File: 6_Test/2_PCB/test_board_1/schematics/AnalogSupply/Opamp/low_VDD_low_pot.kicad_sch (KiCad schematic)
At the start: 4 parts, among them U1 ADA4807-1AKSZ-R7

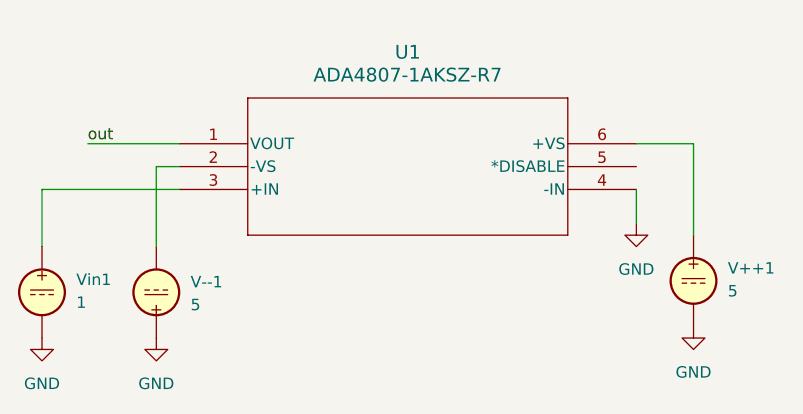
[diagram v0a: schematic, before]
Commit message: progress on op amp. ldo done
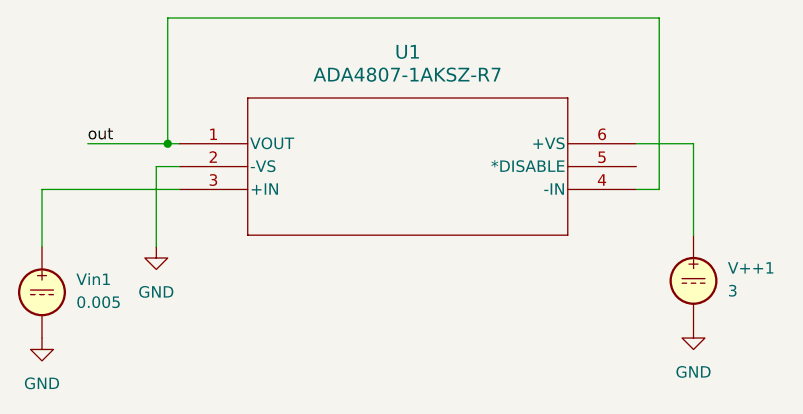
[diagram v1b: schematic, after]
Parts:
- removed V--1: 5, symbol Simulation_SPICE:VDC
- V++1: value 5 -> 3
- Vin1: value 1 -> 0.005
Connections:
- net GND: now also U1.2 (-VS); no longer U1.4 (-IN)
- net out: now also U1.4 (-IN)
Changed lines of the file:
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@@
 	(generator_version "8.0")
 	(paper "A4")
+	(junction
+		(at 125.73 104.14)
+		(diameter 0)
+		(color 0 0 0 0)
+	)
 	(wire
 		(pts
@@
 	(wire
 		(pts
+			(xy 180.34 109.22) (xy 177.8 109.22)
+		)
+		(stroke
+			(width 0)
+			(type default)
+		)
+	)
+	(wire
+		(pts
+			(xy 180.34 90.17) (xy 180.34 109.22)
+		)
+		(stroke
+			(width 0)
+			(type default)
+		)
+	)
+	(wire
+		(pts
 			(xy 124.46 106.68) (xy 127 106.68)
 		)
@@
 	(wire
 		(pts
+			(xy 125.73 104.14) (xy 125.73 90.17)
+		)
+		(stroke
+			(width 0)
+			(type default)
+		)
+	)
+	(wire
+		(pts
 			(xy 184.15 104.14) (xy 184.15 114.3)
 		)
@@
 	(wire
 		(pts
-			(xy 116.84 104.14) (xy 127 104.14)
+			(xy 116.84 104.14) (xy 125.73 104.14)
 		)
 		(stroke
@@
 	(wire
 		(pts
-			(xy 177.8 113.03) (xy 177.8 109.22)
-		)
-		(stroke
-			(width 0)
-			(type default)
-		)
-	)
-	(wire
-		(pts
 			(xy 111.76 109.22) (xy 111.76 115.57)
+		)
+		(stroke
+			(width 0)
+			(type default)
+		)
+	)
+	(wire
+		(pts
+			(xy 125.73 104.14) (xy 127 104.14)
+		)
+		(stroke
+			(width 0)
+			(type default)
+		)
+	)
+	(wire
+		(pts
+			(xy 125.73 90.17) (xy 180.34 90.17)
 		)
 		(stroke
@@
 			)
 		)
-		(property "Value" "5"
+		(property "Value" "3"
 			(at 187.96 120.5201 0)
 			(effects
@@
 				(path "/95e5dcee-77e4-4cc3-9d7c-d0dc3cd96a78"
 					(reference "V++1")
-					(unit 1)
-				)
-			)
-		)
-	)
-	(symbol
-		(lib_id "Simulation_SPICE:VDC")
-		(at 124.46 120.65 180)
-		(unit 1)
-		(exclude_from_sim no)
-		(in_bom yes)
-		(on_board yes)
-		(dnp no)
-		(fields_autoplaced yes)
-		(property "Reference" "V--1"
-			(at 128.27 119.5097 0)
-			(effects
-				(font
-					(size 1.27 1.27)
-				)
-				(justify right)
-			)
-		)
-		(property "Value" "5"
-			(at 128.27 122.0497 0)
-			(effects
-				(font
-					(size 1.27 1.27)
-				)
-				(justify right)
-			)
-		)
-		(property "Footprint" ""
-			(at 124.46 120.65 0)
-			(effects
-				(font
-					(size 1.27 1.27)
-				)
-				(hide yes)
-			)
-		)
-		(property "Datasheet" "https://ngspice.sourceforge.io/docs/ngspice-html-manual/manual.xhtml#sec_Independent_Sources_for"
-			(at 124.46 120.65 0)
-			(effects
-				(font
-					(size 1.27 1.27)
-				)
-				(hide yes)
-			)
-		)
-		(property "Description" "Voltage source, DC"
-			(at 124.46 120.65 0)
-			(effects
-				(font
-					(size 1.27 1.27)
-				)
-				(hide yes)
-			)
-		)
-		(property "Sim.Pins" "1=+ 2=-"
-			(at 124.46 120.65 0)
-			(effects
-				(font
-					(size 1.27 1.27)
-				)
-				(hide yes)
-			)
-		)
-		(property "Sim.Type" "DC"
-			(at 124.46 120.65 0)
-			(effects
-				(font
-					(size 1.27 1.27)
-				)
-				(hide yes)
-			)
-		)
-		(property "Sim.Device" "V"
-			(at 124.46 120.65 0)
-			(effects
-				(font
-					(size 1.27 1.27)
-				)
-				(justify left)
-				(hide yes)
-			)
-		)
-		(pin "2"
-		)
-		(pin "1"
-		)
-		(instances
-			(project "Opamp"
-				(path "/95e5dcee-77e4-4cc3-9d7c-d0dc3cd96a78"
-					(reference "V--1")
-					(unit 1)
-				)
-			)
-		)
-	)
-	(symbol
-		(lib_id "power:GND")
-		(at 177.8 113.03 0)
-		(unit 1)
-		(exclude_from_sim no)
-		(in_bom yes)
-		(on_board yes)
-		(dnp no)
-		(fields_autoplaced yes)
-		(property "Reference" "#PWR03"
-			(at 177.8 119.38 0)
-			(effects
-				(font
-					(size 1.27 1.27)
-				)
-				(hide yes)
-			)
-		)
-		(property "Value" "GND"
-			(at 177.8 118.11 0)
-			(effects
-				(font
-					(size 1.27 1.27)
-				)
-			)
-		)
-		(property "Footprint" ""
-			(at 177.8 113.03 0)
-			(effects
-				(font
-					(size 1.27 1.27)
-				)
-				(hide yes)
-			)
-		)
-		(property "Datasheet" ""
-			(at 177.8 113.03 0)
-			(effects
-				(font
-					(size 1.27 1.27)
-				)
-				(hide yes)
-			)
-		)
-		(property "Description" "Power symbol creates a global label with name \"GND\" , ground"
-			(at 177.8 113.03 0)
-			(effects
-				(font
-					(size 1.27 1.27)
-				)
-				(hide yes)
-			)
-		)
-		(pin "1"
-		)
-		(instances
-			(project ""
-				(path "/95e5dcee-77e4-4cc3-9d7c-d0dc3cd96a78"
-					(reference "#PWR03")
 					(unit 1)
 				)
@@
 			)
 		)
-		(property "Value" "1"
+		(property "Value" "0.005"
 			(at 115.57 121.7901 0)
 			(effects
@@
 	(symbol
 		(lib_id "power:GND")
-		(at 124.46 125.73 0)
+		(at 124.46 115.57 0)
 		(unit 1)
 		(exclude_from_sim no)
@@
 		(fields_autoplaced yes)
 		(property "Reference" "#PWR01"
-			(at 124.46 132.08 0)
+			(at 124.46 121.92 0)
 			(effects
 				(font
@@
 		)
 		(property "Value" "GND"
-			(at 124.46 130.81 0)
+			(at 124.46 120.65 0)
 			(effects
 				(font
@@
 		)
 		(property "Footprint" ""
-			(at 124.46 125.73 0)
+			(at 124.46 115.57 0)
 			(effects
 				(font
@@
 		)
 		(property "Datasheet" ""
-			(at 124.46 125.73 0)
+			(at 124.46 115.57 0)
 			(effects
 				(font
@@
 		)
 		(property "Description" "Power symbol creates a global label with name \"GND\" , ground"
-			(at 124.46 125.73 0)
-			(effects
-				(font
+			(at 124.46 115.57 0)
+			(effects
+				(font

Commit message: ldo and ferrite beads done. working on Opamp.
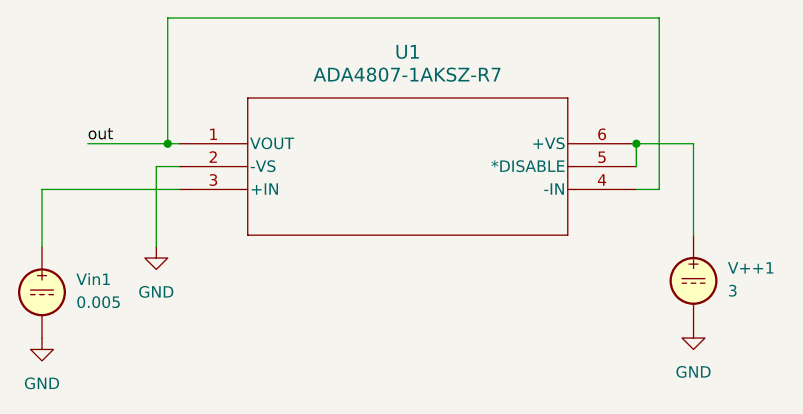
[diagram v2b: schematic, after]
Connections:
- net at U1.6 (+VS), V++1.1: now also U1.5 (*DISABLE)
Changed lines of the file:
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@@
 	(paper "A4")
+	(junction
+		(at 177.8 104.14)
+		(diameter 0)
+		(color 0 0 0 0)
+	)
 	(junction
 		(at 125.73 104.14)
@@
 		(pts
 			(xy 124.46 106.68) (xy 127 106.68)
+		)
+		(stroke
+			(width 0)
+			(type default)
+		)
+	)
+	(wire
+		(pts
+			(xy 177.8 104.14) (xy 177.8 106.68)
 		)
 		(stroke
@@
 			)
 		)
-		(property "Sim.Pins" "1=100 2=101 3=102 4=103 6=104 6=106"
-			(at 127 104.14 0)
-			(effects
+		(property "Sim.Pins" "1=104 2=103 3=100 4=101 5=106 6=102"
+			(at 127 104.14 0)
+			(effects
